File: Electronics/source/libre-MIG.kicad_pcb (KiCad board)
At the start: 2 copper layers, 161.2 x 103.5 mm, 271 parts, among them J1 Conn_01x05, J10 Conn_01x03, J11 Conn_01x08, J12 Conn_01x08, J13 Conn_01x05, J14 Conn_01x03, J15 Conn_01x06, J16 Conn_01x02, J17 Conn_01x06, J18 Conn_01x03, J19 Conn_01x08, J2 Conn_01x03, J20 Conn_01x03, J21 Conn_01x08, J22 Conn_01x04, J23 Conn_01x03, J24 USB_C_Receptacle_USB2.0, J3 Conn_01x03, J4 Conn_01x05, J5 Conn_01x05, J6 Conn_01x20, J7 Conn_01x20, J8 Conn_01x03, J9 Conn_01x03, SW1 SW_Push, SW10 SW_Push, SW11 SW_Push, SW12 SW_Push, SW13 SW_Push, SW14 SW_Coded, SW15 RKJXV1220, SW16 SW_Push, SW17 SKRHABE010, SW18 SKRHABE010, SW2 SW_Push, SW3 SW_Push, SW4 SW_Push, SW5 SW_SPDT, SW6 SW_SPDT, SW7 SW_SPDT, SW8 SW_Push, SW9 SW_Push, U1 STM32F072CBTx, U2 TCA9535PWR, U3 TCA9535PWR, U4 LM2902, U5 ADP122AUJZ-3.3-R7, U6 MAX11613, U7 LM2902, Y1 ABL-8.000MHZ-B2

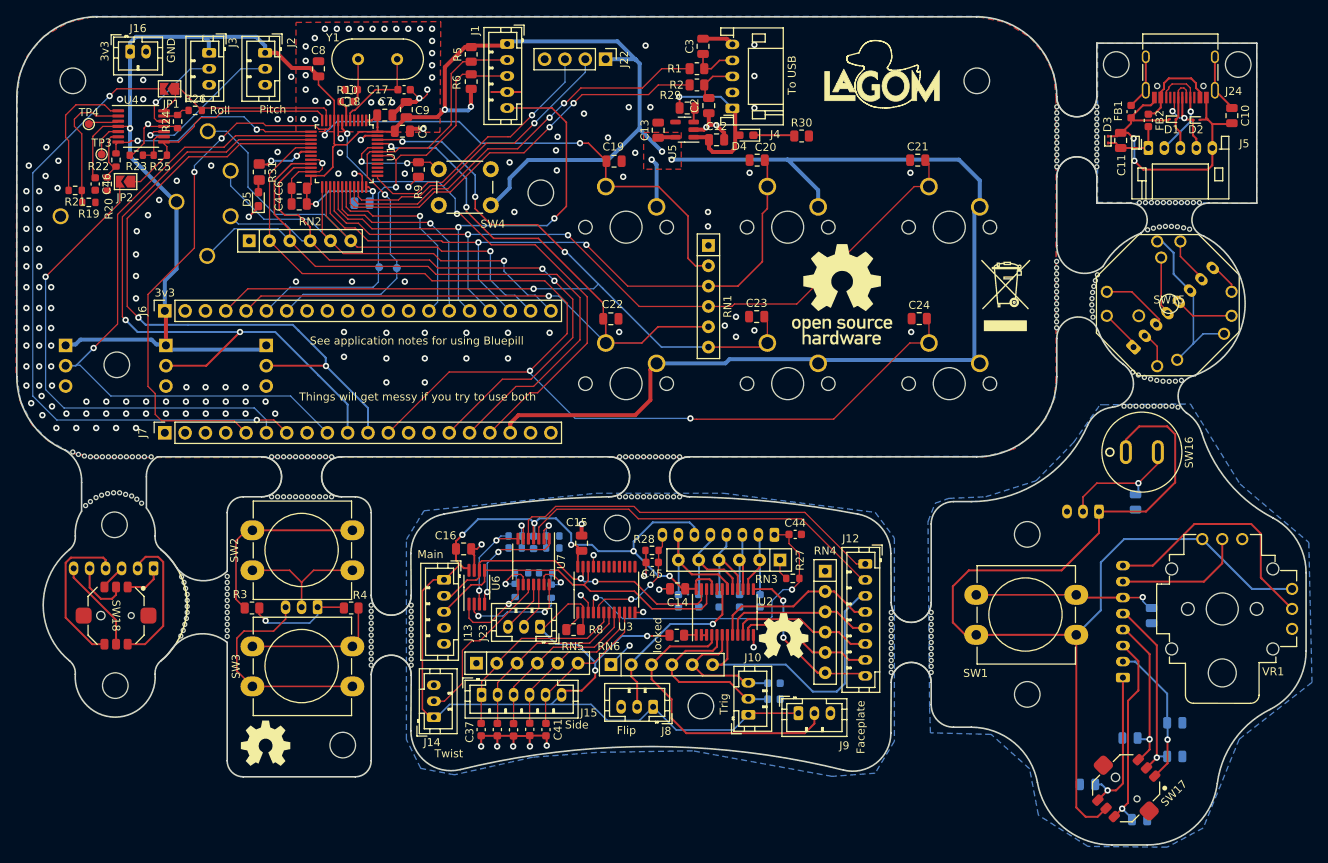
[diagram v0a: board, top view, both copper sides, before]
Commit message: implemented MCP6004/9 and rerouted
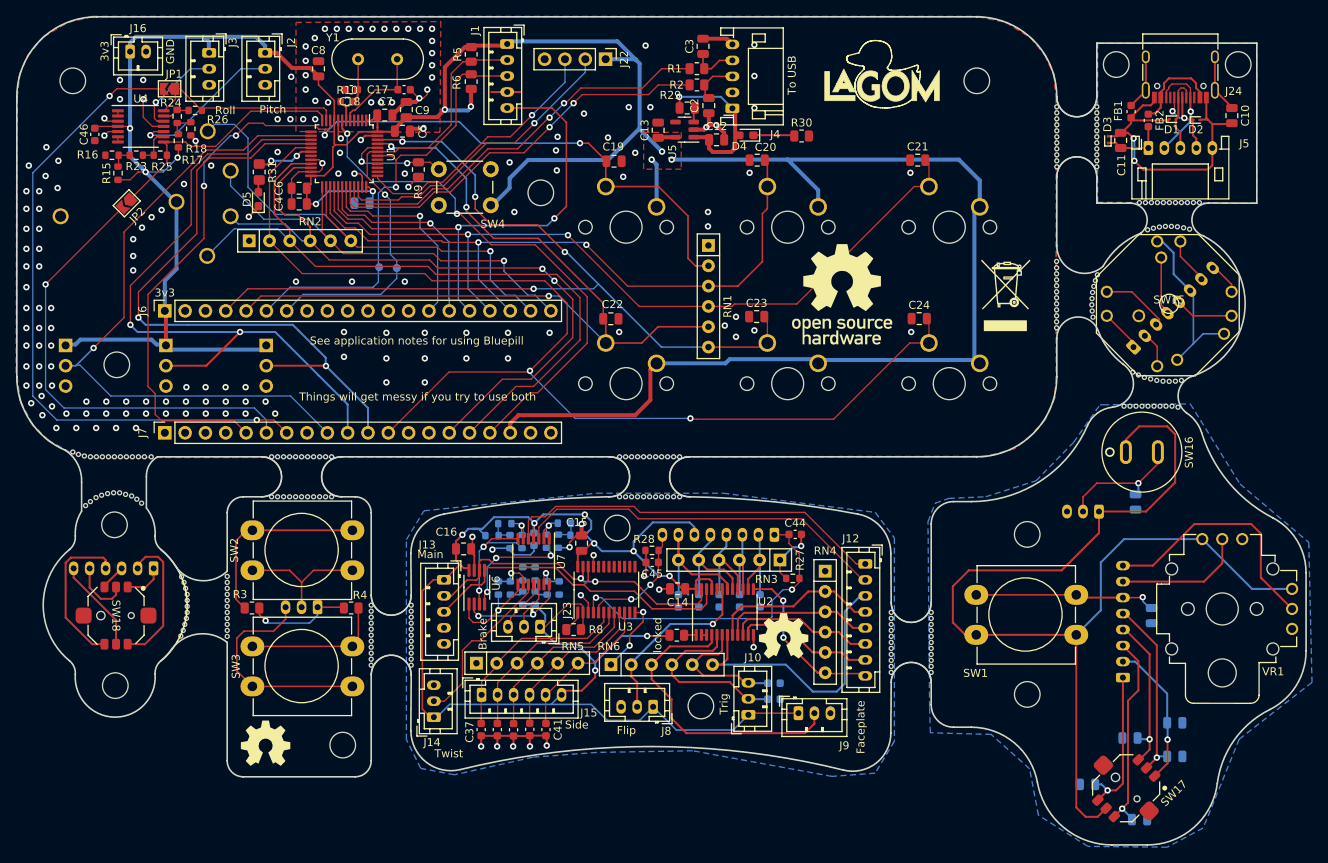
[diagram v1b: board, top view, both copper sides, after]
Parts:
- removed R11, R12, R19, R20: 10k, Resistor_SMD:R_0603_1608Metric
- removed R13, R14, R21, R22: 7.96k, Resistor_SMD:R_0603_1608Metric
- removed TP3, TP4: TestPoint, TestPoint:TestPoint_Pad_D1.0mm
- added R32: 4.7k, Resistor_SMD:R_0603_1608Metric, B.Cu at (187.0, 167.8)
- added R33: 4.7k, Resistor_SMD:R_0603_1608Metric, B.Cu at (184.7, 168.6)
- added R34: 4.7k, Resistor_SMD:R_0603_1608Metric, B.Cu at (176.4, 167.8)
- added R35: 4.7k, Resistor_SMD:R_0603_1608Metric, B.Cu at (178.7, 168.6)
- added R36: 100k, Resistor_SMD:R_0603_1608Metric, B.Cu at (185.4, 166.3)
- added R37: 100k, Resistor_SMD:R_0603_1608Metric, B.Cu at (178.0, 166.3)
- added R38: 110k, Resistor_SMD:R_0603_1608Metric, B.Cu at (183.2, 168.6)
- added R39: 110k, Resistor_SMD:R_0603_1608Metric, B.Cu at (180.2, 168.6)
- added R40: 4.7k, Resistor_SMD:R_0603_1608Metric, B.Cu at (180.2, 175.7)
- added R41: 4.7k, Resistor_SMD:R_0603_1608Metric, B.Cu at (180.2, 172.6)
- added R42: 4.7k, Resistor_SMD:R_0603_1608Metric, B.Cu at (181.8, 175.7)
- added R43: 4.7k, Resistor_SMD:R_0603_1608Metric, B.Cu at (181.8, 172.6)
- added R44: 100k, Resistor_SMD:R_0603_1608Metric, B.Cu at (178.7, 174.4)
- added R45: 100k, Resistor_SMD:R_0603_1608Metric, B.Cu at (183.3, 174.4)
- added R46: 110k, Resistor_SMD:R_0603_1608Metric, B.Cu at (184.8, 174.4)
- added R47: 110k, Resistor_SMD:R_0603_1608Metric, B.Cu at (177.2, 174.4)
- R15, R16: value 10k -> 4.7k; moved to F.Cu
- R17, R18: value 7.96k -> 4.7k; moved to F.Cu
- R23, R24: value 10k -> 100k
- R25, R26: value 7.96k -> 110k
- U4, U7: value LM2902 -> MCP6004
- moved R16 73.8 mm to (128.9, 120.3)
- moved R15 68.3 mm to (129.7, 122.5), turned to 90 degrees
- moved R18 68.1 mm to (138.8, 117.0), turned to -90 degrees
- moved R17 64.9 mm to (137.2, 118.5), turned to 90 degrees
- moved C46 6.20 mm to (126.8, 117.7)
- moved JP2 2.72 mm to (130.7, 126.3), turned to -135 degrees
- moved R24 0.65 mm to (137.1, 115.5)
- moved C47 0.40 mm to (181.7, 168.3)
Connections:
- R15 pad 1: GND -> +3V3
- R16 pad 1: GND -> Net-(R15-Pad2)
- R16 pad 2: Net-(R16-Pad2) -> GND
- R17 pad 1: /IO Controller/Axis1Amp -> +3V3
- R17 pad 2: Net-(R15-Pad2) -> Net-(R17-Pad2)
- R18 pad 1: Net-(R16-Pad2) -> Net-(R17-Pad2)
- R18 pad 2: /IO Controller/Axis2Amp -> GND
- R23 pad 1: GND -> Net-(R15-Pad2)
- R24 pad 1: GND -> Net-(R17-Pad2)
- U1 pad 13: /MCU/ADC3 -> unconnected-(U1-Pad13)
- U4 pad 1: /MCU/ADC2 -> Net-(U4-Pad1)
- U4 pad 2: Net-(R19-Pad2) -> Net-(U4-Pad1)
- U4 pad 3: /MCU/ADC2In -> GND
- U4 pad 5: /MCU/ADC3In -> GND
- U4 pad 6: Net-(R20-Pad2) -> Net-(U4-Pad6)
- U4 pad 7: /MCU/ADC3 -> Net-(U4-Pad6)
- U7 pad 2: Net-(R16-Pad2) -> Net-(R36-Pad2)
- U7 pad 6: Net-(R15-Pad2) -> Net-(R37-Pad2)
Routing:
- net /MCU/ADC3: track 28.1 -> 0.00 mm, vias 2 -> 0
- net GND: track 138.1 -> 161.3 mm, vias 181 -> 184
- net /MCU/ADC2: track 17.0 -> 0.00 mm
- net Net-(R19-Pad2): track 16.8 -> 0.00 mm
- net +3V3: track 735.2 -> 748.4 mm, vias 16 -> 19
- net Net-(R20-Pad2): track 7.12 -> 0.00 mm
- net Net-(R16-Pad2): track 4.82 -> 0.00 mm, vias 1 -> 0
- net Net-(R36-Pad2): track 0.00 -> 4.38 mm, vias 0 -> 1
- net /MCU/ADC3In: track 4.37 -> 0.00 mm
- net Net-(R37-Pad2): track 0.00 -> 4.29 mm, vias 0 -> 1
- net /MCU/ADC2In: track 4.14 -> 0.00 mm
- net /IO Controller/Axis1Amp: track 13.4 -> 17.4 mm
- net Net-(R17-Pad2): track 0.00 -> 3.20 mm
- net Net-(R40-Pad2): track 0.00 -> 3.09 mm
- net /MCU/PitchAmp2: track 60.6 -> 57.5 mm
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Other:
- board text added: "Brake"

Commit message: Redefined face shape to fit panel mount hat; rerouted; DRC check
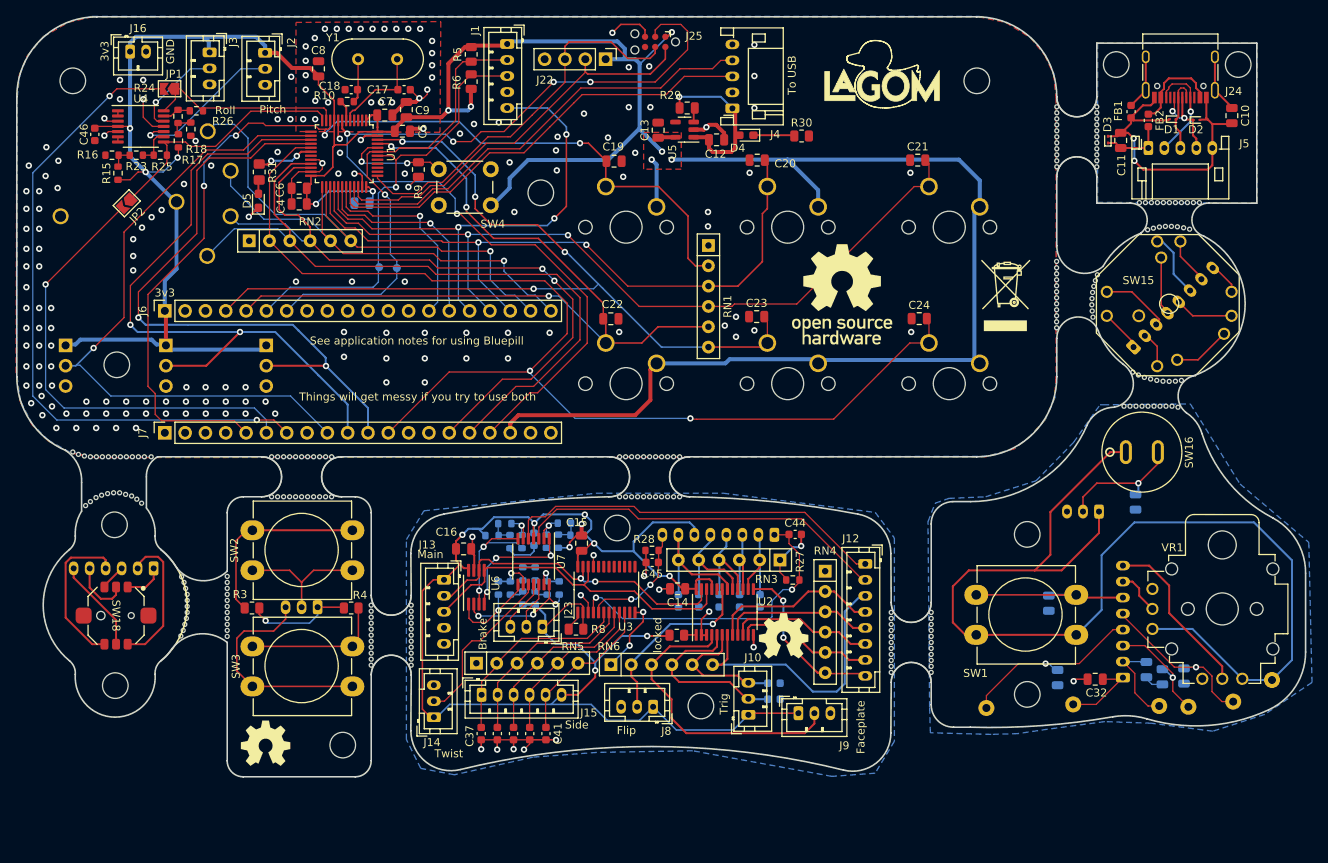
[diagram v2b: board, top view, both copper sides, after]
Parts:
- removed C2, C3: 47pF, Capacitor_SMD:C_0805_2012Metric
- removed R1, R2: 0, Resistor_SMD:R_0805_2012Metric
- removed SW17: SKRHABE010, Personal:SKRHABE010
- added J25: Conn_01x06, Connector:Tag-Connect_TC2030-IDC-NL_2x03_P1.27mm_Vertical, F.Cu at (196.8, 106.1)
- added TP3: TestPoint, TestPoint:TestPoint_Loop_D1.80mm_Drill1.0mm_Beaded, B.Cu at (269.1, 188.6)
- added TP4: TestPoint, TestPoint:TestPoint_Loop_D1.80mm_Drill1.0mm_Beaded, B.Cu at (259.8, 189.2)
- added TP5: TestPoint, TestPoint:TestPoint_Loop_D1.80mm_Drill1.0mm_Beaded, B.Cu at (238.2, 189.4)
- added TP6: TestPoint, TestPoint:TestPoint_Loop_D1.80mm_Drill1.0mm_Beaded, B.Cu at (263.4, 189.2)
- added TP7: TestPoint, TestPoint:TestPoint_Loop_D1.80mm_Drill1.0mm_Beaded, B.Cu at (273.9, 185.9)
- added TP8: TestPoint, TestPoint:TestPoint_Loop_D1.80mm_Drill1.0mm_Beaded, B.Cu at (249.1, 188.9)
- C32: moved to F.Cu
- moved C31 18.1 mm to (260.2, 185.5), turned to -90 degrees
- moved C32 13.2 mm to (251.8, 185.8)
- moved C29 12.9 mm to (246.0, 176.3)
- moved C28 11.8 mm to (247.1, 185.6), turned to -90 degrees
- moved C26 10.1 mm to (262.9, 185.4), turned to -90 degrees
- moved C27 7.54 mm to (258.2, 184.6), turned to -90 degrees
- moved C40 0.53 mm to (181.1, 192.6)
- moved C37 0.50 mm to (175.1, 192.6)
- moved C38 0.50 mm to (177.1, 192.6)
- moved C41 0.50 mm to (183.1, 192.6)
- moved C39 0.47 mm to (179.1, 192.6)
- moved R8 0.30 mm to (186.9, 179.6)
- moved J23 0.30 mm to (182.7, 179.2)
- moved R27 0.20 mm to (214.0, 173.4)
- moved D5 0.20 mm to (147.2, 126.0)
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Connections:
- J4 pad 3: /MCU/ D- -> /MCU/D-
- SW15 pad : (no net) -> GND
- U1 pad 1: unconnected-(U1-Pad1) -> +3V3
- U1 pad 32: /MCU/USB_DM -> /MCU/D-
- U1 pad 33: /MCU/USB_DP -> /MCU/D+
- VR1 pad 2: /Face Plate/Axis2 -> /Face Plate/Axis1
- VR1 pad 5: /Face Plate/Axis1 -> /Face Plate/Axis2
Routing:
- net /MCU/D-: track 0.00 -> 56.8 mm
- net /MCU/NRST: track 65.6 -> 121.2 mm, vias 2 -> 5
- net /MCU/USB_DM: track 51.0 -> 0.00 mm, vias 2 -> 0
- net /MCU/USB_DP: track 50.7 -> 0.00 mm, vias 2 -> 0
- net /MCU/D+: track 5.86 -> 56.5 mm
- net /MCU/SWDCLK: track 33.2 -> 48.2 mm, vias 1 -> 0
- net /MCU/SWDIO: track 38.0 -> 50.3 mm, vias 1 -> 0
- net /Face Plate/DirR: track 25.3 -> 14.5 mm
- net /Face Plate/Axis2: track 16.4 -> 5.64 mm
- net /Face Plate/Axis1: track 30.9 -> 21.2 mm
- net /Face Plate/DirD: track 19.1 -> 10.2 mm, vias 1 -> 0
- net GND: track 161.3 -> 170.0 mm, vias 184 -> 188
- net /Face Plate/DirU: track 18.2 -> 11.0 mm, vias 1 -> 0
- net /MCU/ D-: track 5.85 -> 0.00 mm
- net +3V3: track 748.4 -> 742.7 mm
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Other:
- board size 161.2 x 103.5 mm -> 161.1 x 95 mm

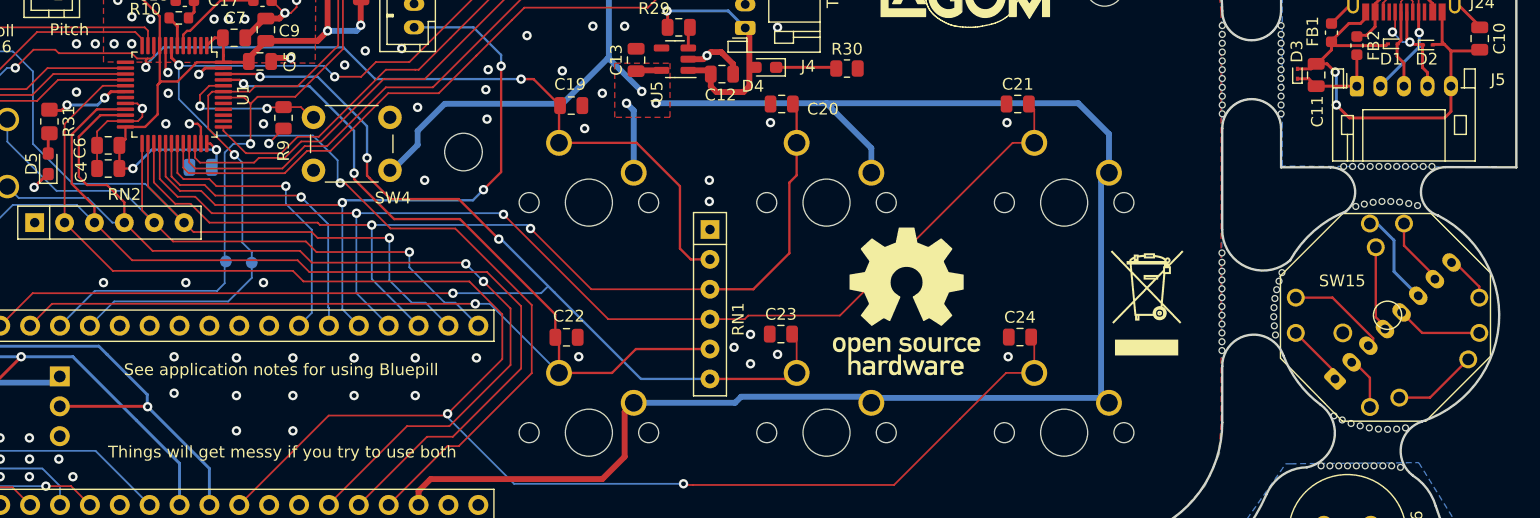
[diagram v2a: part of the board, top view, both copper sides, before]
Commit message: Rev 2 of electronics, full project fabrication outputs
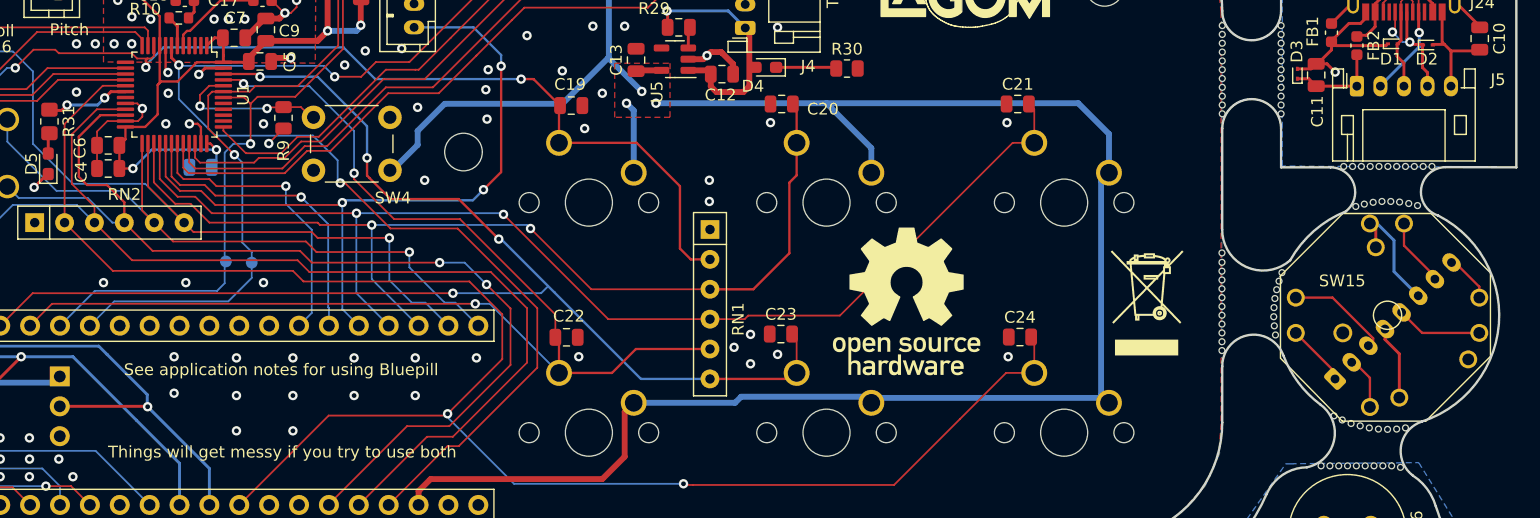
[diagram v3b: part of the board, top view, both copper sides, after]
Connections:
- J4 pad 3: /MCU/D- -> /MCU/ D-
- SW15 pad : GND -> (no net)
- SW15 pad 5: GND -> /Encoder/DirC1
- SW15 pad 6: /Encoder/DirC1 -> +3V3
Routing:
- net GND: track 170.0 -> 147.4 mm, vias 188 -> 187
- net +3V3: track 742.7 -> 744.9 mm
- net /Encoder/DirC1: track 7.62 -> 6.33 mm
- net /MCU/Rot1: track 89.2 -> 89.8 mm
- net /MCU/NRST: track 121.2 -> 121.7 mm
